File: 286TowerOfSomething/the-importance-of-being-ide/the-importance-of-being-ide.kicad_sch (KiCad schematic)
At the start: 55 parts, among them J1 Bus_ISA_16bit, J2 Conn_02x20_Odd_Even, J3 Conn_02x20_Odd_Even, J4 Conn_01x02, J5 Conn_01x02, J6 Conn_01x02, SW1 SW_DIP_x08, U1 SST39SF010, U10 74LS125, U11 74LS125, U12 74LS10, U13 74LS688, U14 74LS07, U2 74LS245, U3 74LS245, U4 74LS245, U5 74LS245, U6 74LS244, U7 GAL16V8, U8 74LS138, U9 74LS04

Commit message: Finishing schematic of the-importance-of-being-ide
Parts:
- added C1, C10, C11, C12, C13, C14, C2, C3, C4, C5, C6, C7, C8, C9: 100n, Capacitor_SMD:C_0603_1608Metric_Pad1.08x0.95mm_HandSolder, symbol Device:C
- added C15: 22u, Capacitor_SMD:CP_Elec_5x5.3, symbol Device:C_Polarized
- D1, D2, D3, D6, D7: footprint Diode_THT:D_DO-35_SOD27_P7.62mm_Horizontal -> Diode_SMD:D_SOD-123
- D4, D5, D8: footprint (none) -> LED_SMD:LED_0603_1608Metric_Pad1.05x0.95mm_HandSolder
- J2, J3: footprint (none) -> Connector_IDC:IDC-Header_2x20_P2.54mm_Vertical
- J4, J5, J6: footprint (none) -> Connector_Molex:Molex_KK-254_AE-6410-02A_1x02_P2.54mm_Vertical
- JP1, JP10, JP2, JP3, JP4, JP9: footprint (none) -> Connector_PinHeader_2.54mm:PinHeader_1x02_P2.54mm_Vertical
- JP5, JP6, JP7, JP8: footprint (none) -> Connector_PinHeader_2.54mm:PinHeader_1x03_P2.54mm_Vertical
- R1, R10, R11, R2, R3, R4, R5, R6, R7, R8, R9: footprint (none) -> Resistor_SMD:R_0603_1608Metric_Pad0.98x0.95mm_HandSolder
- SW1: footprint (none) -> Button_Switch_THT:SW_DIP_SPSTx08_Slide_9.78x22.5mm_W7.62mm_P2.54mm
- U1: footprint (none) -> Package_DIP:DIP-32_W15.24mm
- U10, U11: value 74LS125 -> 74ALS125; footprint (none) -> Package_DIP:DIP-14_W7.62mm
- U12: value 74LS10 -> 74ALS10; footprint (none) -> Package_DIP:DIP-14_W7.62mm
- U13: value 74LS688 -> 74ALS688; footprint (none) -> Package_DIP:DIP-20_W7.62mm
- U14: footprint (none) -> Package_DIP:DIP-14_W7.62mm
- U2, U3, U4, U5: value 74LS245 -> 74ALS245; footprint (none) -> Package_DIP:DIP-20_W7.62mm
- U6: value 74LS244 -> 74ALS244; footprint (none) -> Package_DIP:DIP-20_W7.62mm
- U7: footprint (none) -> Package_DIP:DIP-16_W7.62mm
- U8: value 74LS138 -> 74ALS138; footprint (none) -> Package_DIP:DIP-16_W7.62mm
- U9: value 74LS04 -> 74ALS04; footprint (none) -> Package_DIP:DIP-14_W7.62mm
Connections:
- net +5V: now also U10.14 (VCC), U11.14 (VCC), U12.14 (VCC), U14.14 (VCC), U9.14 (VCC), C1.1, C10.1, C11.1, C12.1, C13.1, C14.1, C15.1, C2.1, C3.1, C4.1, C5.1, C6.1, C7.1, C8.1, C9.1
- net GND: now also U10.7 (GND), U11.7 (GND), U12.7 (GND), U14.7 (GND), U9.7 (GND), C1.2, C10.2, C11.2, C12.2, C13.2, C14.2, C15.2, C2.2, C3.2, C4.2, C5.2, C6.2, C7.2, C8.2, C9.2
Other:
- title: (none) -> The Importance Of Being IDE
- moved on the sheet: D4, D5, D6, D7, D8, J2, J3, J4, J5, J6, JP1, JP10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

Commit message: Started work on IDE layout
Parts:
- U7: footprint Package_DIP:DIP-16_W7.62mm -> Package_DIP:DIP-20_W7.62mm
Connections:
- net +5V: now also RN5.1 (common), U1.32 (VCC), U13.18 (R7), U13.20 (VCC)
- net GND: now also R10.1, R11.2, SW1.11, SW1.12, SW1.13, SW1.14, SW1.15, U1.16 (GND), U1.2 (A16), U13.10 (GND), U13.2 (P0), U13.3 (R0), U13.4 (P1), U13.5 (R1), U13.6 (P2), U13.7 (R2)
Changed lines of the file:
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@@
 	)
 	(junction
+		(at 355.6 199.39)
+		(diameter 0)
+		(color 0 0 0 0)
+	)
+	(junction
 		(at 274.32 156.21)
 		(diameter 0)
@@
 		(color 0 0 0 0)
 	)
+	(junction
+		(at 355.6 123.19)
+		(diameter 0)
+		(color 0 0 0 0)
+	)
 	(no_connect
 		(at 351.79 64.77)
@@
 	(wire
 		(pts
+			(xy 355.6 123.19) (xy 358.14 123.19)
+		)
+		(stroke
+			(width 0)
+			(type default)
+		)
+	)
+	(wire
+		(pts
 			(xy 143.51 144.78) (xy 168.91 144.78)
 		)
@@
 	(wire
 		(pts
+			(xy 355.6 199.39) (xy 355.6 201.93)
+		)
+		(stroke
+			(width 0)
+			(type default)
+		)
+	)
+	(wire
+		(pts
 			(xy 101.6 165.1) (xy 93.98 165.1)
 		)
@@
 	)
 	(symbol
+		(lib_id "power:+5V")
+		(at 358.14 123.19 0)
+		(unit 1)
+		(exclude_from_sim no)
+		(in_bom yes)
+		(on_board yes)
+		(dnp no)
+		(fields_autoplaced yes)
+		(property "Reference" "#PWR021"
+			(at 358.14 127 0)
+			(effects
+				(font
+					(size 1.27 1.27)
+				)
+				(hide yes)
+			)
+		)
+		(property "Value" "+5V"
+			(at 358.14 118.11 0)
+			(effects
+				(font
+					(size 1.27 1.27)
+				)
+			)
+		)
+		(property "Footprint" ""
+			(at 358.14 123.19 0)
+			(effects
+				(font
+					(size 1.27 1.27)
+				)
+				(hide yes)
+			)
+		)
+		(property "Datasheet" ""
+			(at 358.14 123.19 0)
+			(effects
+				(font
+					(size 1.27 1.27)
+				)
+				(hide yes)
+			)
+		)
+		(property "Description" "Power symbol creates a global label with name \"+5V\""
+			(at 358.14 123.19 0)
+			(effects
+				(font
+					(size 1.27 1.27)
+				)
+				(hide yes)
+			)
+		)
+		(pin "1"
+		)
+		(instances
+			(project "the-importance-of-being-ide"
+				(path "/29e749aa-55d9-42fb-8318-49af17b07430"
+					(reference "#PWR021")
+					(unit 1)
+				)
+			)
+		)
+	)
+	(symbol
 		(lib_id "Device:R")
 		(at 208.28 224.79 0)
@@
 			)
 		)
-		(property "Footprint" "Package_DIP:DIP-16_W7.62mm"
+		(property "Footprint" "Package_DIP:DIP-20_W7.62mm"
 			(at 158.75 82.55 0)
 			(effects
@@
 					(unit 1)
 				)
+			)
+		)
+	)
+	(symbol
+		(lib_id "power:GND")
+		(at 355.6 201.93 0)
+		(unit 1)
+		(exclude_from_sim no)
+		(in_bom yes)
+		(on_board yes)
+		(dnp no)
+		(fields_autoplaced yes)
+		(property "Reference" "#PWR022"
+			(at 355.6 208.28 0)
+			(effects
+				(font
+					(size 1.27 1.27)
+				)
+				(hide yes)
+			)
+		)
+		(property "Value" "GND"
+			(at 355.6 207.01 0)
+			(effects
+				(font
+					(size 1.27 1.27)
+				)
+			)
+		)
+		(property "Footprint" ""
+			(at 355.6 201.93 0)
+			(effects
+				(font
+					(size 1.27 1.27)
+				)
+				(hide yes)
+			)
+		)
+		(property "Datasheet" ""
+			(at 355.6 201.93 0)
+			(effects
+				(font
+					(size 1.27 1.27)
+				)
+				(hide yes)
+			)
+		)
+		(property "Description" "Power symbol creates a global label with name \"GND\" , ground"
+			(at 355.6 201.93 0)
+			(effects
+				(font
+					(size 1.27 1.27)
+				)
+				(hide yes)
+			)
+		)
+		(pin "1"
+		)
+		(instances
+			(project "the-importance-of-being-ide"
+				(path "/29e749aa-55d9-42fb-8318-49af17b07430"
+					(reference "#PWR022")
+					(unit 1)
+				)

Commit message: More work on layout of IDE card
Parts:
- J4: value Conn_01x02 -> IDE1_ACT
- J5: value Conn_01x02 -> IDE2_ACT
- J6: value Conn_01x02 -> IDE_ACT
- JP1: value Jumper_2_Open -> IDE1_PWR
- JP10: value Jumper_2_Open -> IDE2_IORDY
- JP2: value Jumper_2_Open -> IDE1_PU
- JP3: value Jumper_2_Open -> IDE2_PU
- JP4: value Jumper_2_Open -> IDE2_PWR
- JP5: value Jumper_3_Open -> IDE1_MODE
- JP6: value Jumper_3_Open -> IDE2_MODE
- JP7: value Jumper_3_Open -> IDE1_CSEL
- JP8: value Jumper_3_Open -> IDE2_CSEL
- JP9: value Jumper_2_Open -> IDE1_IORDY
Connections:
- net ~{IDE1_HI} is gone; now on net ~{IDE1-HI}: U3.19 (CE)
- net ~{IDE1_LO} is gone; now on net ~{IDE1-LO}: U2.19 (CE)
- net ~{IDE2_HI} is gone; now on net ~{IDE2-HI}: U5.19 (CE)
- net ~{IDE2_LO} is gone; now on net ~{IDE2-LO}: U4.19 (CE)
- net IDE2-IORDY: now also JP10.1 (A); no longer JP10.2 (B)
- net IORDY: now also JP10.2 (B); no longer JP10.1 (A)
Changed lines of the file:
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@@
 		)
 	)
-	(label "~{IDE2_LO}"
+	(label "~{IDE2-LO}"
 		(at 93.98 142.24 0)
 		(fields_autoplaced yes)
@@
 		)
 	)
-	(label "~{IDE1_HI}"
+	(label "~{IDE1-HI}"
 		(at 93.98 96.52 0)
 		(fields_autoplaced yes)
@@
 		)
 	)
-	(label "~{IDE2_HI}"
+	(label "~{IDE2-HI}"
 		(at 93.98 187.96 0)
 		(fields_autoplaced yes)
@@
 		)
 	)
-	(label "~{IDE1_LO}"
+	(label "~{IDE1-LO}"
 		(at 93.98 50.8 0)
 		(fields_autoplaced yes)
@@
 			)
 		)
-		(property "Value" "Conn_01x02"
+		(property "Value" "IDE_ACT"
 			(at 294.64 237.4899 0)
 			(effects
@@
 			)
 		)
-		(property "Value" "Jumper_2_Open"
+		(property "Value" "IDE2_PU"
 			(at 358.14 17.78 0)
 			(effects
@@
 			)
 		)
-		(property "Value" "Jumper_3_Open"
+		(property "Value" "IDE2_MODE"
 			(at 308.61 95.2501 90)
 			(effects
@@
 		(lib_id "Jumper:Jumper_2_Open")
 		(at 349.25 115.57 0)
+		(mirror y)
 		(unit 1)
 		(exclude_from_sim yes)
@@
 		(on_board yes)
 		(dnp no)
-		(fields_autoplaced yes)
 		(property "Reference" "JP10"
 			(at 349.25 109.22 0)
@@
 			)
 		)
-		(property "Value" "Jumper_2_Open"
+		(property "Value" "IDE2_IORDY"
 			(at 349.25 111.76 0)
 			(effects
@@
 			)
 		)
-		(property "Value" "Conn_01x02"
+		(property "Value" "IDE2_ACT"
 			(at 256.54 237.4899 0)
 			(effects
@@
 			)
 		)
-		(property "Value" "Jumper_2_Open"
+		(property "Value" "IDE1_PU"
 			(at 298.45 17.78 0)
 			(effects
@@
 			)
 		)
-		(property "Value" "Jumper_3_Open"
+		(property "Value" "IDE1_MODE"
 			(at 283.21 95.2501 90)
 			(effects
@@
 			)
 		)
-		(property "Value" "Jumper_3_Open"
+		(property "Value" "IDE1_CSEL"
 			(at 334.01 95.2501 90)
 			(effects
@@
 			)
 		)
-		(property "Value" "Jumper_2_Open"
+		(property "Value" "IDE2_PWR"
 			(at 377.19 53.34 0)
 			(effects
@@
 			)
 		)
-		(property "Value" "Jumper_3_Open"
+		(property "Value" "IDE2_CSEL"
 			(at 359.41 95.2501 90)
 			(effects
@@
 			)
 		)
-		(property "Value" "Jumper_2_Open"
+		(property "Value" "IDE1_PWR"
 			(at 317.5 53.34 0)
 			(effects
@@
 			)
 		)
-		(property "Value" "Jumper_2_Open"
+		(property "Value" "IDE1_IORDY"
 			(at 298.45 111.76 0)
 			(effects
@@
 			)
 		)
-		(property "Value" "Conn_01x02"
+		(property "Value" "IDE1_ACT"
 			(at 218.44 237.4899 0)
 			(effects

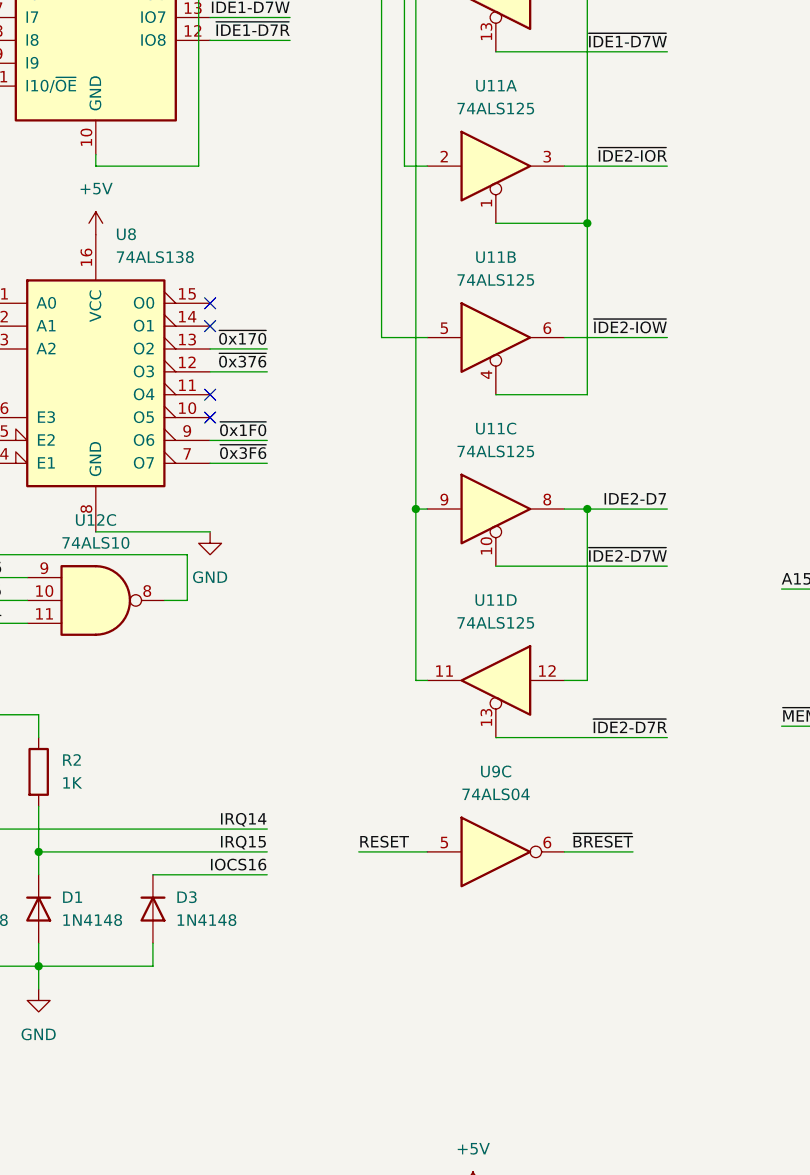
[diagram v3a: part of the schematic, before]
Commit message: Schematic corrections, and layout almost done
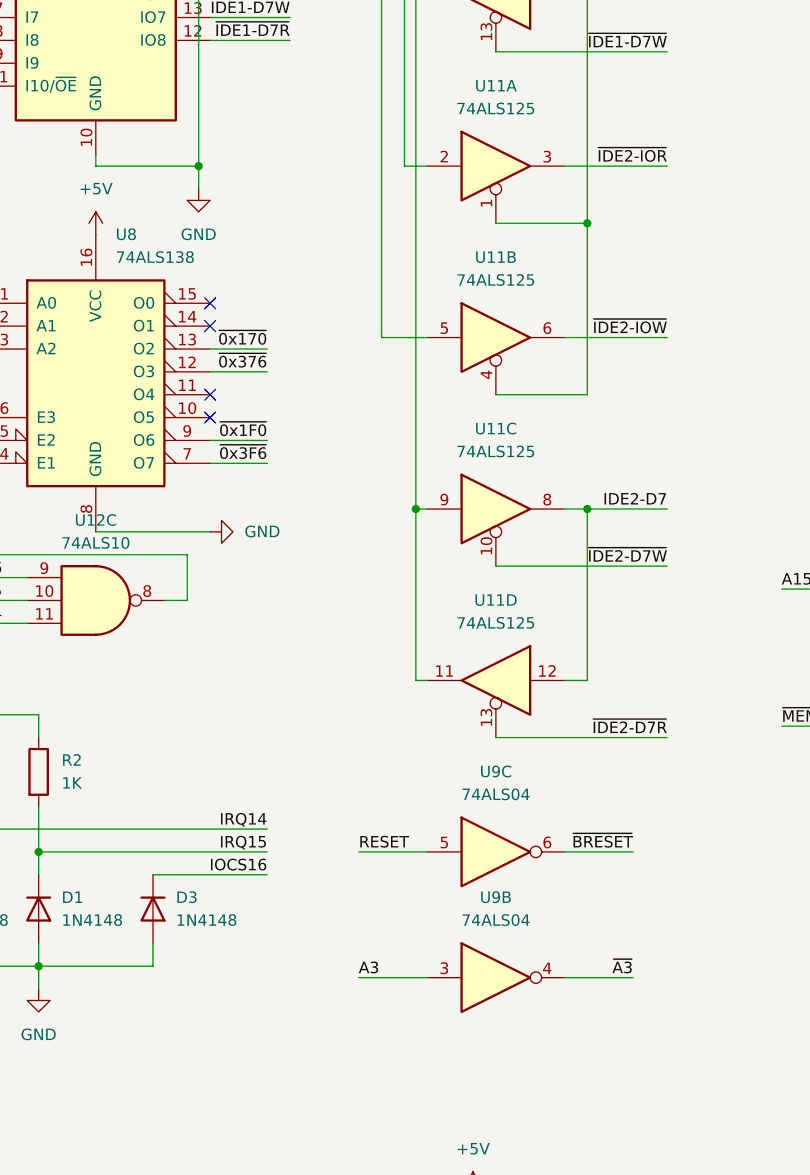
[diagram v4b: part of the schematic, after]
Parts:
- added unit 2 of U9
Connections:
- net A3: now also U9.3
- net GND: now also U6.10 (GND), U7.10 (GND)
- net ~{A3}: now also U9.4
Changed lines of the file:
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@@
 	)
 	(junction
+		(at 170.18 101.6)
+		(diameter 0)
+		(color 0 0 0 0)
+	)
+	(junction
 		(at 152.4 190.5)
 		(diameter 0)
@@
 	(wire
 		(pts
+			(xy 170.18 101.6) (xy 170.18 104.14)
+		)
+		(stroke
+			(width 0)
+			(type default)
+		)
+	)
+	(wire
+		(pts
 			(xy 304.8 123.19) (xy 304.8 128.27)
 		)
@@
 	(wire
 		(pts
+			(xy 218.44 191.77) (xy 210.82 191.77)
+		)
+		(stroke
+			(width 0)
+			(type default)
+		)
+	)
+	(wire
+		(pts
 			(xy 25.4 247.65) (xy 25.4 248.92)
 		)
@@
 	(wire
 		(pts
+			(xy 187.96 191.77) (xy 195.58 191.77)
+		)
+		(stroke
+			(width 0)
+			(type default)
+		)
+	)
+	(wire
+		(pts
 			(xy 350.52 21.59) (xy 350.52 22.86)
 		)
@@
 		)
 	)
+	(label "~{A3}"
+		(at 218.44 191.77 180)
+		(fields_autoplaced yes)
+		(effects
+			(font
+				(size 1.27 1.27)
+			)
+			(justify right bottom)
+		)
+	)
 	(label "A3"
 		(at 332.74 139.7 0)
@@
 		)
 	)
+	(label "A3"
+		(at 187.96 191.77 0)
+		(fields_autoplaced yes)
+		(effects
+			(font
+				(size 1.27 1.27)
+			)
+			(justify left bottom)
+		)
+	)
 	(label "D1"
 		(at 88.9 54.61 180)
@@
 	)
 	(symbol
+		(lib_id "74xx:74LS04")
+		(at 203.2 191.77 0)
+		(unit 2)
+		(exclude_from_sim no)
+		(in_bom yes)
+		(on_board yes)
+		(dnp no)
+		(property "Reference" "U9"
+			(at 203.2 182.88 0)
+			(effects
+				(font
+					(size 1.27 1.27)
+				)
+			)
+		)
+		(property "Value" "74ALS04"
+			(at 203.2 185.42 0)
+			(effects
+				(font
+					(size 1.27 1.27)
+				)
+			)
+		)
+		(property "Footprint" "Package_DIP:DIP-14_W7.62mm"
+			(at 203.2 191.77 0)
+			(effects
+				(font
+					(size 1.27 1.27)
+				)
+				(hide yes)
+			)
+		)
+		(property "Datasheet" "http://www.ti.com/lit/gpn/sn74LS04"
+			(at 203.2 191.77 0)
+			(effects
+				(font
+					(size 1.27 1.27)
+				)
+				(hide yes)
+			)
+		)
+		(property "Description" "Hex Inverter"
+			(at 203.2 191.77 0)
+			(effects
+				(font
+					(size 1.27 1.27)
+				)
+				(hide yes)
+			)
+		)
+		(pin "10"
+		)
+		(pin "3"
+		)
+		(pin "5"
+		)
+		(pin "4"
+		)
+		(pin "12"
+		)
+		(pin "9"
+		)
+		(pin "7"
+		)
+		(pin "13"
+		)
+		(pin "1"
+		)
+		(pin "2"
+		)
+		(pin "6"
+		)
+		(pin "8"
+		)
+		(pin "14"
+		)
+		(pin "11"
+		)
+		(instances
+			(project "the-importance-of-being-ide"
+				(path "/29e749aa-55d9-42fb-8318-49af17b07430"
+					(reference "U9")
+					(unit 2)
+				)
+			)
+		)
+	)
+	(symbol
 		(lib_id "74xx:74LS125")
 		(at 25.4 228.6 0)
@@
 	)
 	(symbol
+		(lib_id "power:GND")
+		(at 170.18 104.14 0)
+		(unit 1)
+		(exclude_from_sim no)
+		(in_bom yes)
+		(on_board yes)
+		(dnp no)
+		(fields_autoplaced yes)
+		(property "Reference" "#PWR023"
+			(at 170.18 110.49 0)
+			(effects
+				(font
+					(size 1.27 1.27)
+				)
+				(hide yes)
+			)
+		)
+		(property "Value" "GND"
+			(at 170.18 109.22 0)
+			(effects
+				(font
+					(size 1.27 1.27)
+				)
+			)
+		)
+		(property "Footprint" ""
+			(at 170.18 104.14 0)
+			(effects
+				(font
+					(size 1.27 1.27)
+				)
+				(hide yes)
+			)
+		)
+		(property "Datasheet" ""
+			(at 170.18 104.14 0)
+			(effects
+				(font
+					(size 1.27 1.27)
+				)
+				(hide yes)
+			)
+		)
+		(property "Description" "Power symbol creates a global label with name \"GND\" , ground"
+			(at 170.18 104.14 0)
+			(effects
+				(font
+					(size 1.27 1.27)
+				)
+				(hide yes)
+			)
+		)
+		(pin "1"
+		)
+		(instances
+			(project "the-importance-of-being-ide"
+				(path "/29e749aa-55d9-42fb-8318-49af17b07430"
+					(reference "#PWR023")
+					(unit 1)
+				)
+			)
+		)
+	)
+	(symbol
 		(lib_id "Jumper:Jumper_3_Open")
 		(at 285.75 96.52 90)
@@
 	(symbol
 		(lib_id "power:GND")
-		(at 171.45 142.24 0)
+		(at 171.45 142.24 90)
 		(unit 1)
 		(exclude_from_sim no)
@@
 		(fields_autoplaced yes)
 		(property "Reference" "#PWR03"
-			(at 171.45 148.59 0)
+			(at 177.8 142.24 0)
 			(effects
 				(font
@@
 		)
 		(property "Value" "GND"
-			(at 171.45 147.32 0)
+			(at 175.26 142.2399 90)
 			(effects
 				(font
 					(size 1.27 1.27)
 				)
+				(justify right)
 			)
 		)

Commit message: Adding bracket to The Importance of Being IDE
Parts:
- added BRACKET1: ~, pc-parts:PC_BRACKET_ISA_KEYSTONE_9202_Rev1, symbol pc-parts:9202
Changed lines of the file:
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@@
+	)
+	(symbol
+		(lib_id "pc-parts:9202")
+		(at 293.37 252.73 0)
+		(unit 1)
+		(exclude_from_sim no)
+		(in_bom yes)
+		(on_board yes)
+		(dnp no)
+		(fields_autoplaced yes)
+		(property "Reference" "BRACKET1"
+			(at 293.37 252.73 0)
+			(effects
+				(font
+					(size 1.27 1.27)
+				)
+				(hide yes)
+			)
+		)
+		(property "Value" "~"
+			(at 298.45 252.73 0)
+			(effects
+				(font
+					(size 1.27 1.27)
+				)
+				(justify left)
+			)
+		)
+		(property "Footprint" "pc-parts:PC_BRACKET_ISA_KEYSTONE_9202_Rev1"
+			(at 293.37 252.73 0)
+			(effects
+				(font
+					(size 1.27 1.27)
+				)
+				(hide yes)
+			)
+		)
+		(property "Datasheet" ""
+			(at 293.37 252.73 0)
+			(effects
+				(font
+					(size 1.27 1.27)
+				)
+				(hide yes)
+			)
+		)
+		(property "Description" ""
+			(at 293.37 252.73 0)
+			(effects
+				(font
+					(size 1.27 1.27)
+				)
+				(hide yes)
+			)
+		)
+		(instances
+			(project ""
+				(path "/29e749aa-55d9-42fb-8318-49af17b07430"
+					(reference "BRACKET1")
+					(unit 1)
+				)
+			)
+		)
 	)
 	(symbol
